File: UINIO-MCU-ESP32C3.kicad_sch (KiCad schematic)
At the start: 43 parts, among them J1 Conn_01x15_Pin, J2 Conn_01x04_Pin, J3 Conn_01x15_Pin, SW1 复位按键, SW2 下载按键, U1 ME6211C33M5G-N, U2 W25Q128JVSSIQ, U3 ESP32-C3, U4 CH343P, Y1 40MHz

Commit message: Release UINIO-MCU-ESP32C3 version 3.5.2.
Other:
- company: 电子技术博客 UinIO.com -> UinIO.com 电子技术实验室
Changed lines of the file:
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@@
   (title_block
     (title "UINIO-MCU-ESP32C3")
-    (date "2023-07-05")
-    (rev "Version 3.5.1")
-    (company "电子技术博客 UinIO.com")
+    (date "2024-01-10")
+    (rev "Version 3.5.2")
+    (company "UinIO.com 电子技术实验室")
   )
   (junction (at 170.18 121.92) (diameter 0) (color 0 0 0 0)

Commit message: Release UINIO-MCU-ESP32C3 version 3.6.0.
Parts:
- removed C6, C8: 0uF, Capacitor_SMD:C_0402_1005Metric, symbol Device:C
- removed L1: 0uH, Inductor_SMD:L_0402_1005Metric, symbol Device:L
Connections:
- net at U3.1 (LNA_IN): now also AE1.1 (FEED)
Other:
- moved on the sheet: AE1
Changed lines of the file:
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@@
   (title_block
     (title "UINIO-MCU-ESP32C3")
-    (date "2024-01-10")
-    (rev "Version 3.5.2")
+    (date "2024-03-05")
+    (rev "Version 3.6.0")
     (company "UinIO.com 电子技术实验室")
   )
@@
   (junction (at 189.23 205.74) (diameter 0) (color 0 0 0 0)
   )
-  (junction (at 161.29 81.28) (diameter 0) (color 0 0 0 0)
-  )
   (junction (at 52.07 222.25) (diameter 0) (color 0 0 0 0)
   )
@@
   )
   (junction (at 102.87 212.09) (diameter 0) (color 0 0 0 0)
-  )
-  (junction (at 173.99 81.28) (diameter 0) (color 0 0 0 0)
   )
   (junction (at 177.8 68.58) (diameter 0) (color 0 0 0 0)
@@
     (stroke (width 0) (type default))
   )
-  (wire (pts (xy 161.29 88.9) (xy 161.29 90.17))
-    (stroke (width 0) (type default))
-  )
   (polyline (pts (xy 127 187.96) (xy 127 271.78))
     (stroke (width 0) (type default))
@@
     (stroke (width 0) (type default))
   )
-  (wire (pts (xy 171.45 81.28) (xy 173.99 81.28))
-    (stroke (width 0) (type default))
-  )
   (wire (pts (xy 367.03 74.93) (xy 370.84 74.93))
     (stroke (width 0) (type default))
@@
     (stroke (width 0) (type default))
   )
-  (wire (pts (xy 151.13 81.28) (xy 161.29 81.28))
-    (stroke (width 0) (type default))
-  )
   (wire (pts (xy 345.44 39.37) (xy 361.95 39.37))
     (stroke (width 0) (type default))
@@
     (stroke (width 0) (type default))
   )
-  (wire (pts (xy 173.99 81.28) (xy 181.61 81.28))
-    (stroke (width 0) (type default))
-  )
   (wire (pts (xy 213.36 76.2) (xy 213.36 63.5))
     (stroke (width 0) (type default))
@@
     (stroke (width 0) (type default))
   )
+  (wire (pts (xy 160.02 81.28) (xy 181.61 81.28))
+    (stroke (width 0) (type default))
+  )
   (wire (pts (xy 52.07 224.79) (xy 44.45 224.79))
     (stroke (width 0) (type default))
@@
     (stroke (width 0) (type default))
   )
-  (wire (pts (xy 146.05 81.28) (xy 146.05 82.55))
+  (wire (pts (xy 154.94 81.28) (xy 154.94 82.55))
     (stroke (width 0) (type default))
   )
@@
     (stroke (width 0) (type default))
   )
-  (wire (pts (xy 173.99 88.9) (xy 173.99 90.17))
-    (stroke (width 0) (type default))
-  )
   (wire (pts (xy 323.85 46.99) (xy 323.85 59.69))
     (stroke (width 0) (type default))
@@
   )
   (polyline (pts (xy 127 104.14) (xy 19.05 104.14))
-    (stroke (width 0) (type default))
-  )
-  (wire (pts (xy 161.29 81.28) (xy 163.83 81.28))
     (stroke (width 0) (type default))
   )
@@
     )
   )
-  (symbol (lib_id "Device:C") (at 173.99 85.09 0) (unit 1)
-    (in_bom yes) (on_board yes) (dnp no)
-    (property "Reference" "C8" (at 176.53 85.09 0)
-      (effects (font (size 1.27 1.27)) (justify left))
-    )
-    (property "Value" "0uF" (at 173.99 87.63 0)
-      (effects (font (size 1.27 1.27)) (justify left))
-    )
-    (property "Footprint" "Capacitor_SMD:C_0402_1005Metric" (at 174.9552 88.9 0)
-      (effects (font (size 1.27 1.27)) hide)
-    )
-    (property "Datasheet" "~" (at 173.99 85.09 0)
-      (effects (font (size 1.27 1.27)) hide)
-    )
-    (pin "1")
-    (pin "2")
-    (instances
-      (project "UINIO-MCU-ESP32C3"
-        (path "/50397beb-4ccc-41d0-957c-018e540a45ce"
-          (reference "C8") (unit 1)
-        )
-      )
-    )
-  )
   (symbol (lib_id "Device:C") (at 189.23 234.95 180) (unit 1)
     (in_bom yes) (on_board yes) (dnp no)
@@
     )
   )
-  (symbol (lib_id "Device:Antenna_Chip") (at 148.59 78.74 0) (mirror y) (unit 1)
-    (in_bom yes) (on_board yes) (dnp no)
-    (property "Reference" "AE1" (at 144.145 70.485 0)
+  (symbol (lib_id "Device:Antenna_Chip") (at 157.48 78.74 0) (mirror y) (unit 1)
+    (in_bom yes) (on_board yes) (dnp no)
+    (property "Reference" "AE1" (at 153.035 70.485 0)
       (effects (font (size 1.27 1.27)) (justify right))
     )
-    (property "Value" "Antenna_Chip" (at 147.955 75.565 0)
+    (property "Value" "Antenna_Chip" (at 156.845 75.565 0)
       (effects (font (size 1.27 1.27)) (justify right))
     )
-    (property "Footprint" "RF_Antenna:Texas_SWRA117D_2.4GHz_Right" (at 151.13 74.295 0)
-      (effects (font (size 1.27 1.27)) hide)
-    )
-    (property "Datasheet" "~" (at 151.13 74.295 0)
+    (property "Footprint" "RF_Antenna:Texas_SWRA117D_2.4GHz_Right" (at 160.02 74.295 0)
+      (effects (font (size 1.27 1.27)) hide)
+    )
+    (property "Datasheet" "~" (at 160.02 74.295 0)
       (effects (font (size 1.27 1.27)) hide)
     )
@@
         (path "/50397beb-4ccc-41d0-957c-018e540a45ce"
           (reference "Y1") (unit 1)
-        )
-      )
-    )
-  )
-  (symbol (lib_id "Device:C") (at 161.29 85.09 0) (unit 1)
-    (in_bom yes) (on_board yes) (dnp no)
-    (property "Reference" "C6" (at 163.83 85.09 0)
-      (effects (font (size 1.27 1.27)) (justify left))
-    )
-    (property "Value" "0uF" (at 161.29 87.63 0)
-      (effects (font (size 1.27 1.27)) (justify left))
-    )
-    (property "Footprint" "Capacitor_SMD:C_0402_1005Metric" (at 162.2552 88.9 0)
-      (effects (font (size 1.27 1.27)) hide)
-    )
-    (property "Datasheet" "~" (at 161.29 85.09 0)
-      (effects (font (size 1.27 1.27)) hide)
-    )
-    (pin "1")
-    (pin "2")
-    (instances
-      (project "UINIO-MCU-ESP32C3"
-        (path "/50397beb-4ccc-41d0-957c-018e540a45ce"
-          (reference "C6") (unit 1)
         )
       )
@@
         (path "/50397beb-4ccc-41d0-957c-018e540a45ce"
           (reference "C3") (unit 1)
-        )
-      )
-    )
-  )
-  (symbol (lib_id "power:GND") (at 173.99 90.17 0) (unit 1)
-    (in_bom yes) (on_board yes) (dnp no)
-    (property "Reference" "#PWR0129" (at 173.99 96.52 0)
-      (effects (font (size 1.27 1.27)) hide)
-    )
-    (property "Value" "GND" (at 173.99 93.98 0)
-      (effects (font (size 1.27 1.27)))
-    )
-    (property "Footprint" "" (at 173.99 90.17 0)
-      (effects (font (size 1.27 1.27)) hide)
-    )
-    (property "Datasheet" "" (at 173.99 90.17 0)
-      (effects (font (size 1.27 1.27)) hide)
-    )
-    (pin "1")
-    (instances
-      (project "UINIO-MCU-ESP32C3"
-        (path "/50397beb-4ccc-41d0-957c-018e540a45ce"
-          (reference "#PWR0129") (unit 1)
         )
       )
@@
     )
   )
-  (symbol (lib_id "power:GND") (at 161.29 90.17 0) (unit 1)
-    (in_bom yes) (on_board yes) (dnp no)
-    (property "Reference" "#PWR0128" (at 161.29 96.52 0)
-      (effects (font (size 1.27 1.27)) hide)
-    )
-    (property "Value" "GND" (at 161.29 93.98 0)
-      (effects (font (size 1.27 1.27)))
-    )
-    (property "Footprint" "" (at 161.29 90.17 0)
-      (effects (font (size 1.27 1.27)) hide)
-    )
-    (property "Datasheet" "" (at 161.29 90.17 0)
-      (effects (font (size 1.27 1.27)) hide)
-    )
-    (pin "1")
-    (instances
-      (project "UINIO-MCU-ESP32C3"
-        (path "/50397beb-4ccc-41d0-957c-018e540a45ce"
-          (reference "#PWR0128") (unit 1)
-        )
-      )
-    )
-  )
   (symbol (lib_id "power:GND") (at 367.03 138.43 270) (unit 1)
     (in_bom yes) (on_board yes) (dnp no)
@@
     )
   )
-  (symbol (lib_id "power:GND") (at 146.05 82.55 0) (unit 1)
-    (in_bom yes) (on_board yes) (dnp no)
-    (property "Reference" "#PWR0126" (at 146.05 88.9 0)
-      (effects (font (size 1.27 1.27)) hide)
-    )
-    (property "Value" "GND" (at 146.05 86.36 0)
-      (effects (font (size 1.27 1.27)))
-    )
-    (property "Footprint" "" (at 146.05 82.55 0)
-      (effects (font (size 1.27 1.27)) hide)
-    )
-    (property "Datasheet" "" (at 146.05 82.55 0)
+  (symbol (lib_id "power:GND") (at 154.94 82.55 0) (unit 1)
+    (in_bom yes) (on_board yes) (dnp no)
+    (property "Reference" "#PWR0126" (at 154.94 88.9 0)
+      (effects (font (size 1.27 1.27)) hide)
+    )
+    (property "Value" "GND" (at 154.94 86.36 0)
+      (effects (font (size 1.27 1.27)))
+    )
+    (property "Footprint" "" (at 154.94 82.55 0)
+      (effects (font (size 1.27 1.27)) hide)
+    )
+    (property "Datasheet" "" (at 154.94 82.55 0)
       (effects (font (size 1.27 1.27)) hide)
     )
@@
         )
       )
-    )
-  )
-  (symbol (lib_id "Device:L") (at 167.64 81.28 90) (unit 1)
-    (in_bom yes) (on_board yes) (dnp no)
-    (property "Reference" "L1" (at 168.275 78.74 90)
-      (effects (font (size 1.27 1.27)))
-    )
-    (property "Value" "0uH" (at 168.275 82.55 90)
-      (effects (font (size 1.27 1.27)))
-    )
-    (property "Footprint" "Inductor_SMD:L_0402_1005Metric" (at 167.64 81.28 0)
-      (effects (font (size 1.27 1.27)) hide)
-    )
-    (property "Datasheet" "~" (at 167.64 81.28 0)
-      (effects (font (size 1.27 1.27)) hide)
-    )
-    (pin "1")
-    (pin "2")
-    (instances
-      (project "UINIO-MCU-ESP32C3"
-        (path "/50397beb-4ccc-41d0-957c-018e540a45ce"
-          (reference "L1") (unit 1)
-        )
-      )

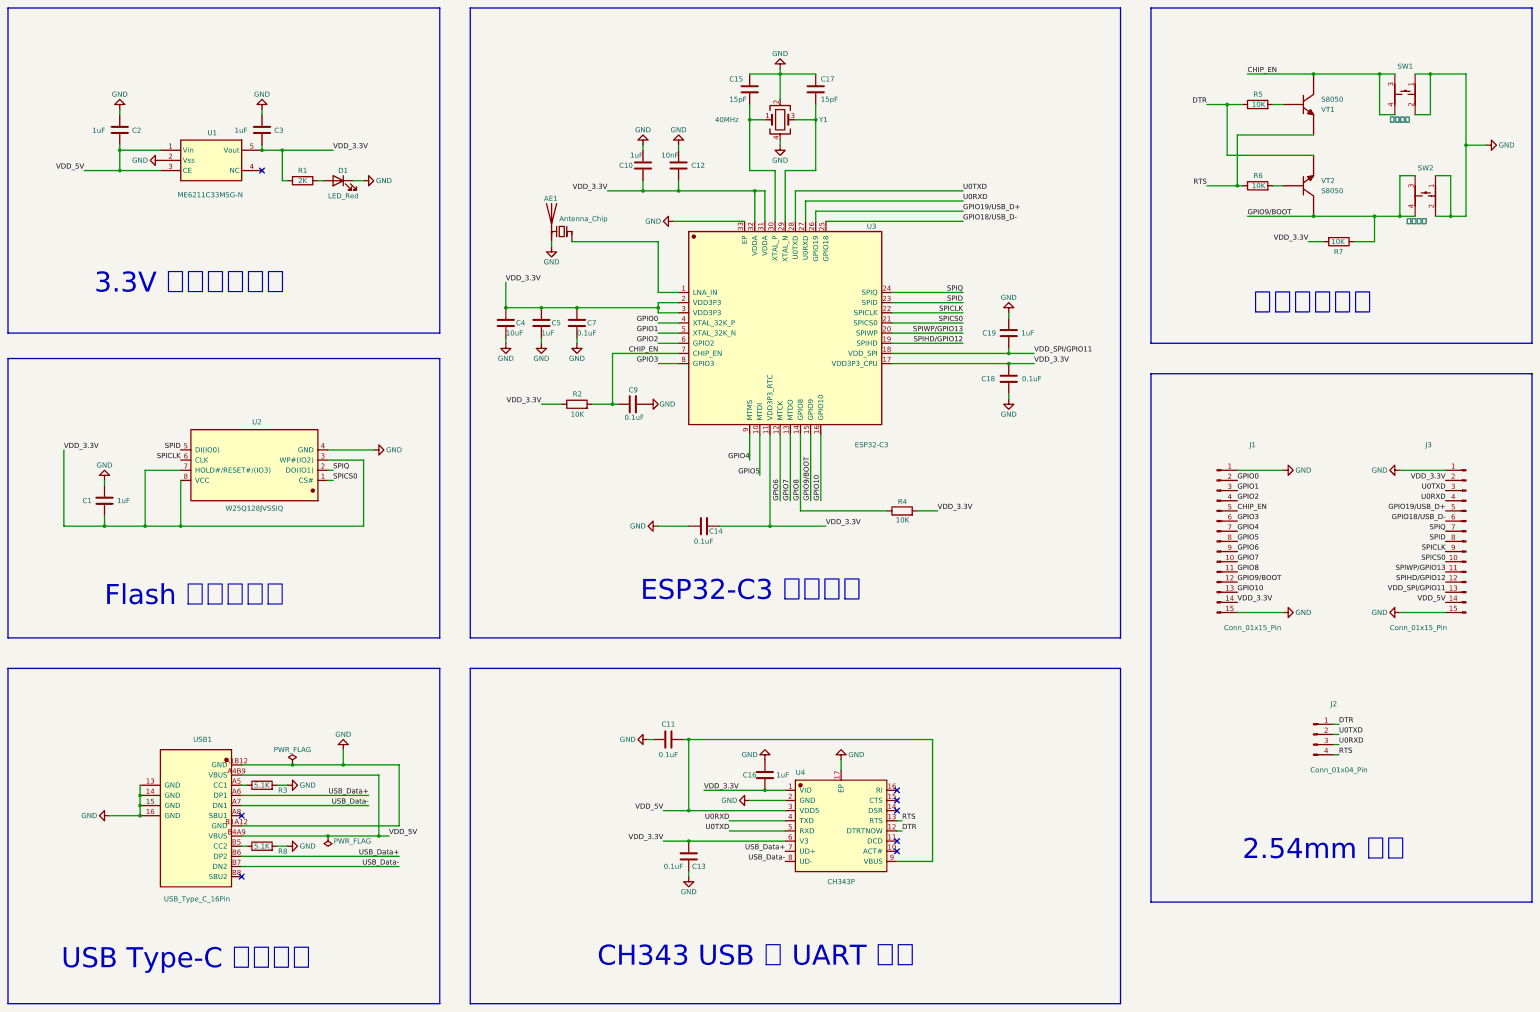
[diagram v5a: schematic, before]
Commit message: Replace PCB layout.
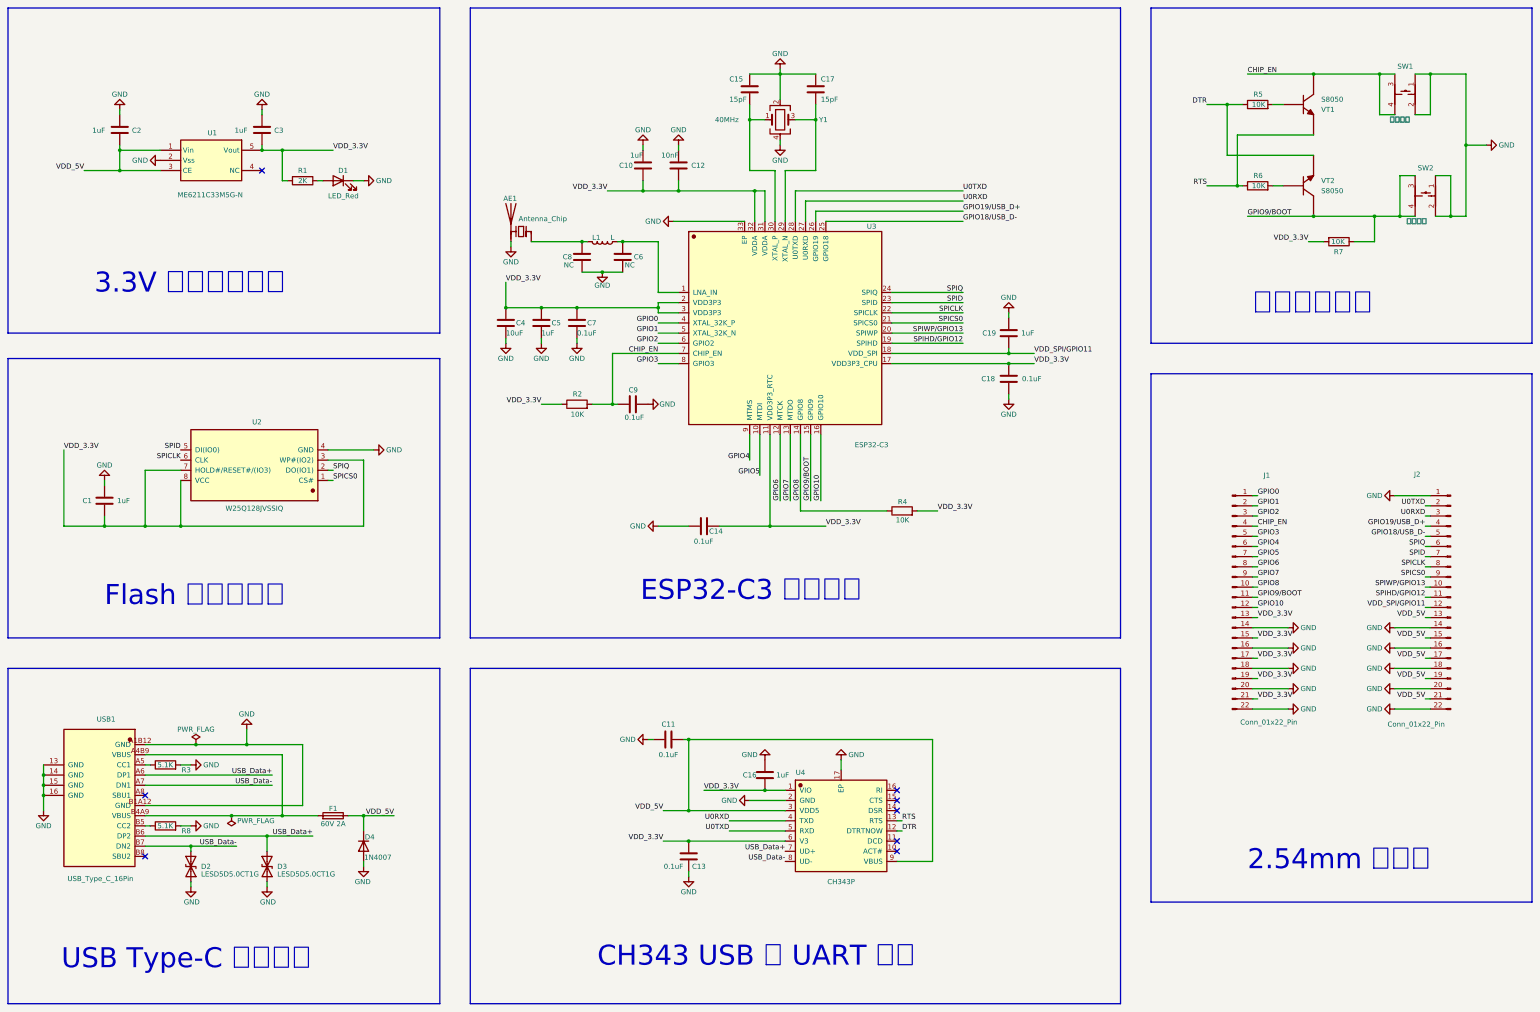
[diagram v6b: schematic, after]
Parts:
- removed J1, J3: Conn_01x15_Pin, Connector_PinHeader_2.54mm:PinHeader_1x15_P2.54mm_Vertical, symbol Connector:Conn_01x15_Pin
- removed J2: Conn_01x04_Pin, Connector_PinHeader_2.54mm:PinHeader_1x04_P2.54mm_Vertical, symbol Connector:Conn_01x04_Pin
- added C6, C8: NC, Capacitor_SMD:C_0402_1005Metric, symbol Device:C
- added D2, D3: LESD5D5.0CT1G, Diode_SMD:D_SOD-523, symbol Diode:1N630xCA
- added D4: 1N4007, Diode_SMD:Nexperia_CFP3_SOD-123W, symbol Diode:1N4007
- added F1: 60V 2A, Fuse:Fuse_1206_3216Metric, symbol Device:Fuse
- added J1, J2: Conn_01x22_Pin, Connector_PinHeader_2.54mm:PinHeader_1x22_P2.54mm_Vertical, symbol Connector:Conn_01x22_Pin
- added L1: L, Inductor_SMD:L_0402_1005Metric, symbol Device:L
- C2, C3: footprint Capacitor_SMD:C_0402_1005Metric -> Capacitor_SMD:C_0603_1608Metric
- R1, R3, R8: footprint Resistor_SMD:R_0402_1005Metric -> Resistor_SMD:R_0603_1608Metric
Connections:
- net CHIP_EN: now also J1.4 (Pin_4)
- net GND: now also C6.2, C8.2, D2.1 (A1), D3.1 (A1), D4.2 (A), J1.14 (Pin_14), J1.16 (Pin_16), J1.18 (Pin_18), J1.20 (Pin_20), J1.22 (Pin_22), J2.1 (Pin_1), J2.14 (Pin_14), J2.16 (Pin_16), J2.18 (Pin_18), J2.20 (Pin_20), J2.22 (Pin_22)
- net GPIO0: now also J1.1 (Pin_1)
- net GPIO1: now also J1.2 (Pin_2)
- net GPIO10: now also J1.12 (Pin_12)
- net GPIO18/USB_D-: now also J2.5 (Pin_5)
- net GPIO19/USB_D+: now also J2.4 (Pin_4)
- net GPIO2: now also J1.3 (Pin_3)
- net GPIO3: now also J1.5 (Pin_5)
- net GPIO4: now also J1.6 (Pin_6)
- net GPIO5: now also J1.7 (Pin_7)
- net GPIO6: now also J1.8 (Pin_8)
- net GPIO7: now also J1.9 (Pin_9)
- net GPIO8: now also J1.10 (Pin_10)
- net GPIO9/BOOT: now also J1.11 (Pin_11)
- net SPICLK: now also J2.8 (Pin_8)
- net SPICS0: now also J2.9 (Pin_9)
- net SPID: now also J2.7 (Pin_7)
- net SPIHD/GPIO12: now also J2.11 (Pin_11)
- net SPIQ: now also J2.6 (Pin_6)
- net SPIWP/GPIO13: now also J2.10 (Pin_10)
- net U0RXD: now also J2.3 (Pin_3)
- net U0TXD: now also J2.2 (Pin_2)
- net USB_Data+: now also D3.2 (A2)
- net USB_Data-: now also D2.2 (A2)
- net VDD_3.3V: now also J1.13 (Pin_13), J1.15 (Pin_15), J1.17 (Pin_17), J1.19 (Pin_19), J1.21 (Pin_21)
- net VDD_5V: now also D4.1 (K), F1.1, J2.13 (Pin_13), J2.15 (Pin_15), J2.17 (Pin_17), J2.19 (Pin_19), J2.21 (Pin_21); no longer USB1.A4B9 (VBUS), USB1.B4A9 (VBUS)
- net VDD_SPI/GPIO11: now also J2.12 (Pin_12)
- net at AE1.1 (FEED): now also C8.1, L1.2; no longer U3.1 (LNA_IN)
- new net: F1.2, USB1.A4B9 (VBUS), USB1.B4A9 (VBUS)
- new net: C6.1, L1.1, U3.1 (LNA_IN)
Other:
- note added: "2.54mm 杜邦针"
- note removed: "2.54mm 排针"
- moved on the sheet: AE1, R3, R8, USB1

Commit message: Update PCB layout.
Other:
- moved on the sheet: C15
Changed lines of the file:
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@@
 	)
 	(junction
+		(at 203.2 50.8)
+		(diameter 0)
+		(color 0 0 0 0)
+	)
+	(junction
 		(at 323.85 46.99)
 		(diameter 0)
@@
 	)
 	(junction
-		(at 204.47 50.8)
-		(diameter 0)
-		(color 0 0 0 0)
-	)
-	(junction
 		(at 74.93 224.79)
 		(diameter 0)
@@
 	(wire
 		(pts
-			(xy 204.47 46.99) (xy 204.47 50.8)
+			(xy 203.2 46.99) (xy 203.2 50.8)
 		)
 		(stroke
@@
 	(wire
 		(pts
-			(xy 204.47 39.37) (xy 212.09 39.37)
+			(xy 203.2 39.37) (xy 212.09 39.37)
 		)
 		(stroke
@@
 	(wire
 		(pts
-			(xy 204.47 50.8) (xy 204.47 63.5)
+			(xy 203.2 50.8) (xy 203.2 63.5)
 		)
 		(stroke
@@
 	(wire
 		(pts
+			(xy 203.2 50.8) (xy 208.28 50.8)
+		)
+		(stroke
+			(width 0)
+			(type default)
+		)
+	)
+	(wire
+		(pts
 			(xy 83.82 242.57) (xy 83.82 241.3)
 		)
@@
 	(wire
 		(pts
-			(xy 204.47 63.5) (xy 210.82 63.5)
+			(xy 203.2 63.5) (xy 210.82 63.5)
 		)
 		(stroke
@@
 	(wire
 		(pts
-			(xy 204.47 50.8) (xy 208.28 50.8)
-		)
-		(stroke
-			(width 0)
-			(type default)
-		)
-	)
-	(wire
-		(pts
 			(xy 196.85 152.4) (xy 209.55 152.4)
 		)
@@
 		)
 		(property "Value" "GND"
-			(at 180.34 76.2 90)
+			(at 180.594 76.454 90)
 			(effects
 				(font
@@
 	(symbol
 		(lib_id "Device:C")
-		(at 204.47 43.18 0)
+		(at 203.2 43.18 0)
 		(unit 1)
 		(exclude_from_sim no)
@@
 		(dnp no)
 		(property "Reference" "C15"
-			(at 199.39 40.64 0)
+			(at 198.12 40.64 0)
 			(effects
 				(font
@@
 		)
 		(property "Value" "15pF"
-			(at 199.39 45.72 0)
+			(at 198.12 45.72 0)
 			(effects
 				(font
@@
 		)
 		(property "Footprint" "Capacitor_SMD:C_0402_1005Metric"
-			(at 205.4352 46.99 0)
+			(at 204.1652 46.99 0)
 			(effects
 				(font
@@
 		)
 		(property "Datasheet" "~"
-			(at 204.47 43.18 0)
+			(at 203.2 43.18 0)
 			(effects
 				(font
@@
 		)
 		(property "Description" ""
-			(at 204.47 43.18 0)
+			(at 203.2 43.18 0)
 			(effects
 				(font

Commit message: Update PCB layout.
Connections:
- net VDD_3.3V: now also D4.1 (K), F1.1; no longer C3.2, R1.2, U1.5 (Vout)
- net VDD_5V: now also USB1.A4B9 (VBUS), USB1.B4A9 (VBUS); no longer D4.1 (K), F1.1
- new net: C3.2, F1.2, R1.2, U1.5 (Vout)
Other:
- moved on the sheet: AE1, C10, C12, C14, C15, C17, C18, C19, C2, C3, C4, C5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
